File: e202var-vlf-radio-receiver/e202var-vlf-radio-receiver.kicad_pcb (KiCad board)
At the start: 2 copper layers, 0 parts

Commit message: Rough part placement. Created README. Images made by gerbv are off-center.
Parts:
- added BNC1: 12/18V, Wickerlib:CONN-BNC-TECONN-1-1634612-0, F.Cu at (106.1, 110.5)
- added BNC2: ANT IN, Wickerlib:CONN-BNC-TECONN-1-1634612-0, F.Cu at (107.4, 47.0)
- added BNC3: LINE IN/OUT, Wickerlib:CONN-BNC-TECONN-1-1634612-0, F.Cu at (106.1, 94.0)
- added C1: 33nF, Wickerlib:CAP-DISC-D7.5MM-P5MM, F.Cu at (65.3, 91.7)
- added C10: 10nF, Wickerlib:CAP-DISC-D3MM-P2.5MM, F.Cu at (89.9, 64.5)
- added C11: 100nF, Wickerlib:CAP-DISC-D7.5MM-P5MM, F.Cu at (72.6, 103.1)
- added C12: 10uF, Wickerlib:CAP-DISC-D3MM-P2.5MM, F.Cu at (80.5, 98.3)
- added C13: 100uF, Wickerlib:CAP-DISC-D7.5MM-P5MM, F.Cu at (65.3, 85.3)
- added C15: 150pF, Wickerlib:CAP-DISC-D3MM-P2.5MM, F.Cu at (82.5, 65.3)
- added C16: 4.7nF, Wickerlib:CAP-DISC-D7.5MM-P5MM, F.Cu at (64.8, 102.9)
- added C2: 100nF, Wickerlib:CAP-DISC-D7.5MM-P5MM, F.Cu at (72.7, 51.3)
- added C3: 8.2pF, Wickerlib:CAP-DISC-D7.5MM-P5MM, F.Cu at (62.7, 67.1)
- added C4: 10uF, Wickerlib:CAP-DISC-D3MM-P2.5MM, F.Cu at (74.2, 83.3)
- added C5: 150pF, Wickerlib:CAP-DISC-D3MM-P2.5MM, F.Cu at (86.6, 89.4)
- added C6: 10uF, Wickerlib:CAP-DISC-D3MM-P2.5MM, F.Cu at (103.6, 77.5)
- added C7: 4.7nF, Wickerlib:CAP-DISC-D7.5MM-P5MM, F.Cu at (99.3, 81.8)
- added C8: 150pF, Wickerlib:CAP-DISC-D3MM-P2.5MM, F.Cu at (61.7, 73.2)
- added C9: 100uF, Wickerlib:CAP-DISC-D7.5MM-P5MM, F.Cu at (98.0, 60.2)
- added D1: 1N4001, Wickerlib:DIODE-DO-41, F.Cu at (82.6, 115.8)
- added D2: 1N4001, Wickerlib:DIODE-DO-41, F.Cu at (95.5, 99.1)
- added D3: BLUE, Wickerlib:LED-D5MM-2PIN, F.Cu at (67.3, 114.8)
- added J1: 9V, Wickerlib:CONN-BARREL-JACK-2.5x5.5MM-TH, F.Cu at (60.9, 111.1)
- added J2: ON/OFF, Wickerlib:CONN-ONSHORE-SCREW-GREEN-2PIN-TH, F.Cu at (75.2, 114.6)
- added J3: HEADPHONES, Wickerlib:SJ1-3523N, F.Cu at (109.2, 60.7)
- added J4: 12V/18V, Wickerlib:CONN-BARREL-JACK-2.5x5.5MM-TH, F.Cu at (90.7, 109.5)
- added J5: FILTER, Wickerlib:CONN-ONSHORE-SCREW-GREEN-2PIN-TH, F.Cu at (57.1, 101.1)
- added L1: 3.3UH, Wickerlib:IND-78F-AXIAL, F.Cu at (76.5, 50.8)
- added LAMP1: NEON, Wickerlib:CONN-HEADER-STRAIGHT-P2.54MM-1x02, F.Cu at (93.7, 51.1)
- added Q1: BC547, Wickerlib:TO-92-INLINE-NARROW-OVAL, F.Cu at (74.2, 96.0)
- added Q2: BC547, Wickerlib:TO-92-INLINE-NARROW-OVAL, F.Cu at (63.5, 56.4)
- added R1: 10M, Wickerlib:RES-CARBONFILM-7MM, F.Cu at (79.0, 56.4)
- added R10: 10K, Wickerlib:RES-TRIMPOT-TTELEC-P160-TH, F.Cu at (111.8, 72.4)
- added R11: 4.7K, Wickerlib:RES-CARBONFILM-7MM, F.Cu at (90.2, 98.6)
- added R12: 2.2K, Wickerlib:RES-CARBONFILM-7MM, F.Cu at (73.2, 108.7)
- added R13: 1K, Wickerlib:RES-CARBONFILM-7MM, F.Cu at (69.8, 103.9)
- added R17: 33, Wickerlib:RES-CARBONFILM-7MM, F.Cu at (67.6, 78.5)
- added R2: 100K, Wickerlib:RES-CARBONFILM-7MM, F.Cu at (70.9, 40.4)
- added R3: 100K, Wickerlib:RES-CARBONFILM-7MM, F.Cu at (83.1, 69.3)
- added R4: 3.3k, Wickerlib:RES-CARBONFILM-7MM, F.Cu at (69.3, 85.1)
- added R5: 10M, Wickerlib:RES-CARBONFILM-7MM, F.Cu at (80.0, 45.2)
- added R6: 100K, Wickerlib:RES-CARBONFILM-7MM, F.Cu at (84.1, 50.5)
- added R7: 10, Wickerlib:RES-CARBONFILM-7MM, F.Cu at (84.3, 59.9)
- added R8: 10K, Wickerlib:RES-CARBONFILM-7MM, F.Cu at (95.2, 82.8)
- added R9: 33, Wickerlib:RES-CARBONFILM-7MM, F.Cu at (91.7, 55.4)
- added SMA1: ANT IN, Wickerlib:CONN-SMA-STRAIGHT-TH, F.Cu at (94.5, 43.2)
- added U1: MC7809, Wickerlib:TO-220-NEUTRAL123-VERT-LONGPADS, F.Cu at (90.7, 104.9)
- added U2: TLE2426, Wickerlib:TO-92-INLINE-NARROW-OVAL, F.Cu at (74.4, 91.2)
- added U3: NJM386, Wickerlib:DIP-8-W7.62MM-LONGPADS, F.Cu at (69.3, 63.0)
- added U4: TL081CP, Wickerlib:DIP-8-W7.62MM-LONGPADS, F.Cu at (81.3, 76.7)
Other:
- board outline added: 55.9 x 81.3 mm

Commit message: Added parts. Ready for layout.
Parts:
- added REF**: HOLE-PLATED-3.2MM, Wickerlib:HOLE-PLATED-3.2MM, F.Cu at (85.1, 33.5)
- added REF**: HOLE-PLATED-3.2MM, Wickerlib:HOLE-PLATED-3.2MM, F.Cu at (91.4, 33.5)
- added REF**: HOLE-PLATED-3.2MM, Wickerlib:HOLE-PLATED-3.2MM, F.Cu at (97.8, 33.5)
- L1: footprint Wickerlib:IND-78F-AXIAL -> Wickerlib:RES-CARBONFILM-7MM
- moved J3 4.32 mm to (107.2, 64.5)
- moved SMA1 3.75 mm to (91.2, 45.0)
- moved L1 2.65 mm to (75.7, 48.3), turned to 180 degrees
- moved LAMP1 2.50 mm to (96.0, 52.1)
- moved BNC2 1.05 mm to (106.7, 46.2)
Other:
- board text added: "12/9/2016"
- board text added: "E202VAR VLF Natural Radio Receiver"
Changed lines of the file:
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@@
 (kicad_pcb (version 4) (host pcbnew 4.0.4+e1-6308~48~ubuntu16.04.1-stable)
   (general
-    (links 87)
-    (no_connects 87)
-    (area 0 0 0 0)
+    (links 94)
+    (no_connects 94)
+    (area 58.343799 38.023799 114.376201 119.456201)
     (thickness 1.6)
-    (drawings 22)
+    (drawings 28)
     (tracks 0)
     (zones 0)
-    (modules 49)
+    (modules 52)
     (nets 33)
   )
@@
   )
   (module Wickerlib:CONN-BNC-TECONN-1-1634612-0 (layer F.Cu)
-    (at 107.4166 46.96968 270)
+    (at 106.6546 46.24578 270)
     (descr "BNC Socket TYCO AMP")
     (tags "BNC Socket TYCO AMP")
@@
       (net 29 "Net-(J1-Pad1)"))
   )
-  (module Wickerlib:SJ1-3523N (layer F.Cu)
-    (at 109.22 60.706)
-    (fp_text reference J3 (at 0 0.5) (layer F.SilkS)
-      (effects (font (size 1 1) (thickness 0.15)))
-    )
-    (fp_text value HEADPHONES (at 0 -0.5) (layer F.Fab)
-      (effects (font (size 1 1) (thickness 0.15)))
-    )
-  )
   (module Wickerlib:CONN-BARREL-JACK-2.5x5.5MM-TH (layer F.Cu)
     (at 90.651 109.5224 90)
@@
       (net 5 +2V))
   )
-  (module Wickerlib:IND-78F-AXIAL (layer F.Cu)
-    (at 76.454 50.8)
-    (fp_text reference L1 (at 7.112 -0.254) (layer F.SilkS)
-      (effects (font (size 1 1) (thickness 0.15)))
-    )
-    (fp_text value 3.3UH (at 0 -0.5) (layer F.Fab)
-      (effects (font (size 1 1) (thickness 0.15)))
-    )
-  )
   (module Wickerlib:CONN-HEADER-STRAIGHT-P2.54MM-1x02 (layer F.Cu)
-    (at 93.726 51.054 270)
+    (at 96.012 52.07 270)
     (descr "Through hole pin header")
     (tags "pin header")
@@
   )
   (module Wickerlib:CONN-SMA-STRAIGHT-TH (layer F.Cu)
-    (at 94.488 43.18)
+    (at 91.186 44.958)
     (descr "SMA pcb mounting jack")
     (tags "SMA Jack  Striaght")
@@
     (pad 8 thru_hole oval (at 7.62 0) (size 2.3 1.6) (drill 0.8) (layers *.Cu *.Mask F.SilkS))
   )
+  (module Wickerlib:RES-CARBONFILM-7MM (layer F.Cu)
+    (at 75.692 48.26 180)
+    (descr "Resistor, Axial,  RM 7.62mm, 1/3W,")
+    (tags "Resistor Axial RM 7.62mm 1/3W R3")
+    (fp_text reference L1 (at 3.8 0 180) (layer F.Fab)
+      (effects (font (size 1 1) (thickness 0.15)))
+    )
+    (fp_text value 3.3UH (at 3.81 3.81 180) (layer F.Fab) hide
+      (effects (font (size 1 1) (thickness 0.15)))
+    )
+    (fp_text user %R (at 3.9 -2.3 180) (layer F.SilkS)
+      (effects (font (size 1 1) (thickness 0.15)))
+    )
+    (fp_line (start 8.9 -1.5) (end -1.3 -1.5) (layer F.Fab) (width 0.0508))
+    (fp_line (start 8.9 1.5) (end 8.9 -1.5) (layer F.Fab) (width 0.0508))
+    (fp_line (start 8.8 1.5) (end 8.9 1.5) (layer F.Fab) (width 0.0508))
+    (fp_line (start -1.3 1.5) (end 8.8 1.5) (layer F.Fab) (width 0.0508))
+    (fp_line (start -1.3 -1.5) (end -1.3 1.5) (layer F.Fab) (width 0.0508))
+    (fp_line (start -1.25 -1.5) (end 8.85 -1.5) (layer F.CrtYd) (width 0.05))
+    (fp_line (start -1.25 1.5) (end -1.25 -1.5) (layer F.CrtYd) (width 0.05))
+    (fp_line (start 8.85 -1.5) (end 8.85 1.5) (layer F.CrtYd) (width 0.05))
+    (fp_line (start -1.25 1.5) (end 8.85 1.5) (layer F.CrtYd) (width 0.05))
+    (fp_line (start 1.27 -1.27) (end 6.35 -1.27) (layer F.SilkS) (width 0.15))
+    (fp_line (start 6.35 -1.27) (end 6.35 1.27) (layer F.SilkS) (width 0.15))
+    (fp_line (start 6.35 1.27) (end 1.27 1.27) (layer F.SilkS) (width 0.15))
+    (fp_line (start 1.27 1.27) (end 1.27 -1.27) (layer F.SilkS) (width 0.15))
+    (pad 1 thru_hole circle (at 0 0 180) (size 1.99898 1.99898) (drill 1.00076) (layers *.Cu *.SilkS *.Mask)
+      (net 3 "Net-(BNC2-Pad1)"))
+    (pad 2 thru_hole circle (at 7.62 0 180) (size 1.99898 1.99898) (drill 1.00076) (layers *.Cu *.SilkS *.Mask)
+      (net 7 "Net-(C2-Pad2)"))
+  )
+  (module Wickerlib:HOLE-PLATED-3.2MM (layer F.Cu)
+    (at 85.09 33.528)
+    (fp_text reference REF** (at 0 0) (layer F.Fab)
+      (effects (font (size 1 1) (thickness 0.15)))
+    )
+    (fp_text value HOLE-PLATED-3.2MM (at 0 -0.5) (layer F.Fab) hide
+      (effects (font (size 1 1) (thickness 0.15)))
+    )
+    (fp_circle (center 0 0) (end 2.54 1.27) (layer F.Fab) (width 0.04064))
+    (pad 1 thru_hole circle (at 0 0) (size 5 5) (drill 3.2) (layers *.Cu *.Mask))
+  )
+  (module Wickerlib:HOLE-PLATED-3.2MM (layer F.Cu)
+    (at 91.44 33.528)
+    (fp_text reference REF** (at 0 0) (layer F.Fab)
+      (effects (font (size 1 1) (thickness 0.15)))
+    )
+    (fp_text value HOLE-PLATED-3.2MM (at 0 -0.5) (layer F.Fab) hide
+      (effects (font (size 1 1) (thickness 0.15)))
+    )
+    (fp_circle (center 0 0) (end 2.54 1.27) (layer F.Fab) (width 0.04064))
+    (pad 1 thru_hole circle (at 0 0) (size 5 5) (drill 3.2) (layers *.Cu *.Mask))
+  )
+  (module Wickerlib:HOLE-PLATED-3.2MM (layer F.Cu)
+    (at 97.79 33.528)
+    (fp_text reference REF** (at 0 0) (layer F.Fab)
+      (effects (font (size 1 1) (thickness 0.15)))
+    )
+    (fp_text value HOLE-PLATED-3.2MM (at 0 -0.5) (layer F.Fab) hide
+      (effects (font (size 1 1) (thickness 0.15)))
+    )
+    (fp_circle (center 0 0) (end 2.54 1.27) (layer F.Fab) (width 0.04064))
+    (pad 1 thru_hole circle (at 0 0) (size 5 5) (drill 3.2) (layers *.Cu *.Mask))
+  )
+  (module Wickerlib:SJ1-3523N (layer F.Cu)
+    (at 107.188 64.516)
+    (fp_text reference J3 (at 1.27 -2.413) (layer F.Fab)
+      (effects (font (size 1 1) (thickness 0.15)))
+    )
+    (fp_text value HEADPHONES (at 0 -0.5) (layer F.Fab) hide
+      (effects (font (size 1 1) (thickness 0.15)))
+    )
+    (fp_text user %R (at -1.778 -9.779) (layer F.SilkS)
+      (effects (font (size 1 1) (thickness 0.15)))
+    )
+    (fp_line (start -3.81 3.81) (end 6.35 3.81) (layer F.CrtYd) (width 0.04064))
+    (fp_line (start -3.81 -8.89) (end -3.81 3.81) (layer F.CrtYd) (width 0.04064))
+    (fp_line (start 6.35 -8.89) (end -3.81 -8.89) (layer F.CrtYd) (width 0.04064))
+    (fp_line (start 6.35 3.81) (end 6.35 -8.89) (layer F.CrtYd) (width 0.04064))
+    (fp_line (start -3.81 3.81) (end 6.35 3.81) (layer F.Fab) (width 0.04064))
+    (fp_line (start -3.81 -8.89) (end -3.81 3.81) (layer F.Fab) (width 0.04064))
+    (fp_line (start 6.35 -8.89) (end -3.81 -8.89) (layer F.Fab) (width 0.04064))
+    (fp_line (start 6.35 -8.89) (end 6.35 3.81) (layer F.Fab) (width 0.04064))
+    (fp_line (start -3.81 3.81) (end 6.35 3.81) (layer F.SilkS) (width 0.1524))
+    (fp_line (start -3.81 -8.89) (end -3.81 3.81) (layer F.SilkS) (width 0.1524))
+    (fp_line (start 6.35 -8.89) (end -3.81 -8.89) (layer F.SilkS) (width 0.1524))
+    (fp_line (start 6.35 3.81) (end 6.35 -8.89) (layer F.SilkS) (width 0.1524))
+    (pad 4 thru_hole circle (at 5.08 -7.62) (size 2.1844 2.1844) (drill 1.2954) (layers *.Cu *.Mask)
+      (net 1 GND))
+    (pad 3 thru_hole circle (at 5.08 -5.08) (size 2.1844 2.1844) (drill 1.2954) (layers *.Cu *.Mask)
+      (net 1 GND))
+    (pad "" np_thru_hole circle (at 5.08 -2.54) (size 1.2954 1.2954) (drill 1.2954) (layers *.Cu))
+    (pad 2 thru_hole circle (at 5.08 0) (size 2.1844 2.1844) (drill 1.2954) (layers *.Cu *.Mask)
+      (net 17 "Net-(C9-Pad1)"))
+    (pad 1 thru_hole circle (at 5.08 2.54) (size 2.1844 2.1844) (drill 1.2954) (layers *.Cu *.Mask)
+      (net 17 "Net-(C9-Pad1)"))
+    (pad 5 thru_hole circle (at 0 -2.54) (size 2.1844 2.1844) (drill 1.2954) (layers *.Cu *.Mask)
+      (net 1 GND))
+    (pad "" np_thru_hole circle (at 0 -7.62) (size 1.2954 1.2954) (drill 1.2954) (layers *.Cu))
+    (pad "" np_thru_hole circle (at -2.54 -7.62) (size 1.2954 1.2954) (drill 1.2954) (layers *.Cu))
+    (pad "" np_thru_hole circle (at 0 2.54) (size 1.2954 1.2954) (drill 1.2954) (layers *.Cu))
+    (pad "" np_thru_hole circle (at -2.54 2.54) (size 1.2954 1.2954) (drill 1.2954) (layers *.Cu))
+  )
+  (gr_text 12/9/2016 (at 109.22 30.734) (layer F.Fab)
+    (effects (font (size 1.016 1.016) (thickness 0.1524)))
+  )
+  (gr_text "E202VAR VLF Natural Radio Receiver" (at 99.568 28.702) (layer F.Fab)
+    (effects (font (size 1.016 1.016) (thickness 0.1524)))
+  )
+  (gr_line (start 58.42 38.1) (end 114.3 38.1) (layer F.Fab) (width 0.1524))
+  (gr_line (start 58.42 119.38) (end 58.42 38.1) (layer F.Fab) (width 0.1524))
+  (gr_line (start 114.3 119.38) (end 58.42 119.38) (layer F.Fab) (width 0.1524))
+  (gr_line (start 114.3 38.1) (end 114.3 119.38) (layer F.Fab) (width 0.1524))
   (gr_line (start 113.03 38.1) (end 114.3 38.1) (layer Edge.Cuts) (width 0.1524))
   (gr_line (start 58.42 38.1) (end 113.03 38.1) (layer Edge.Cuts) (width 0.1524))

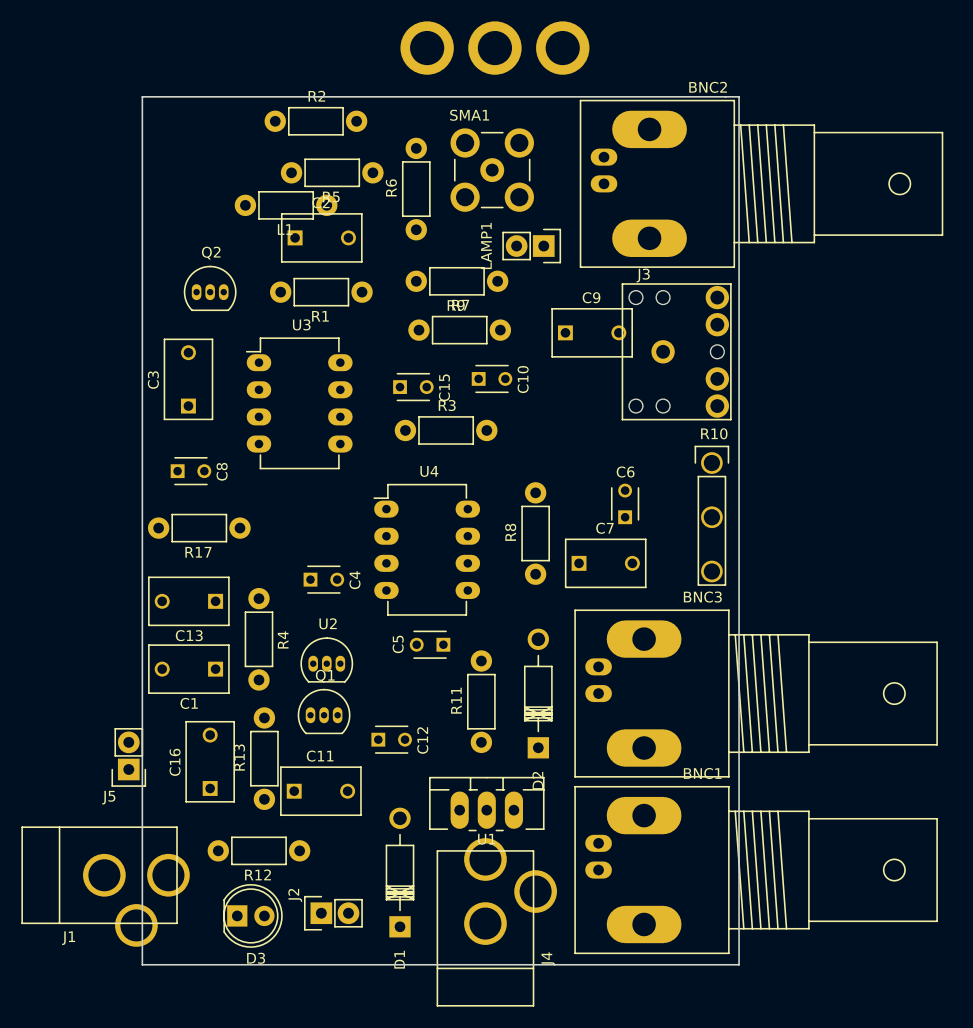
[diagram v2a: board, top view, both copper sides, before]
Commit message: Ported the board to KiCad.
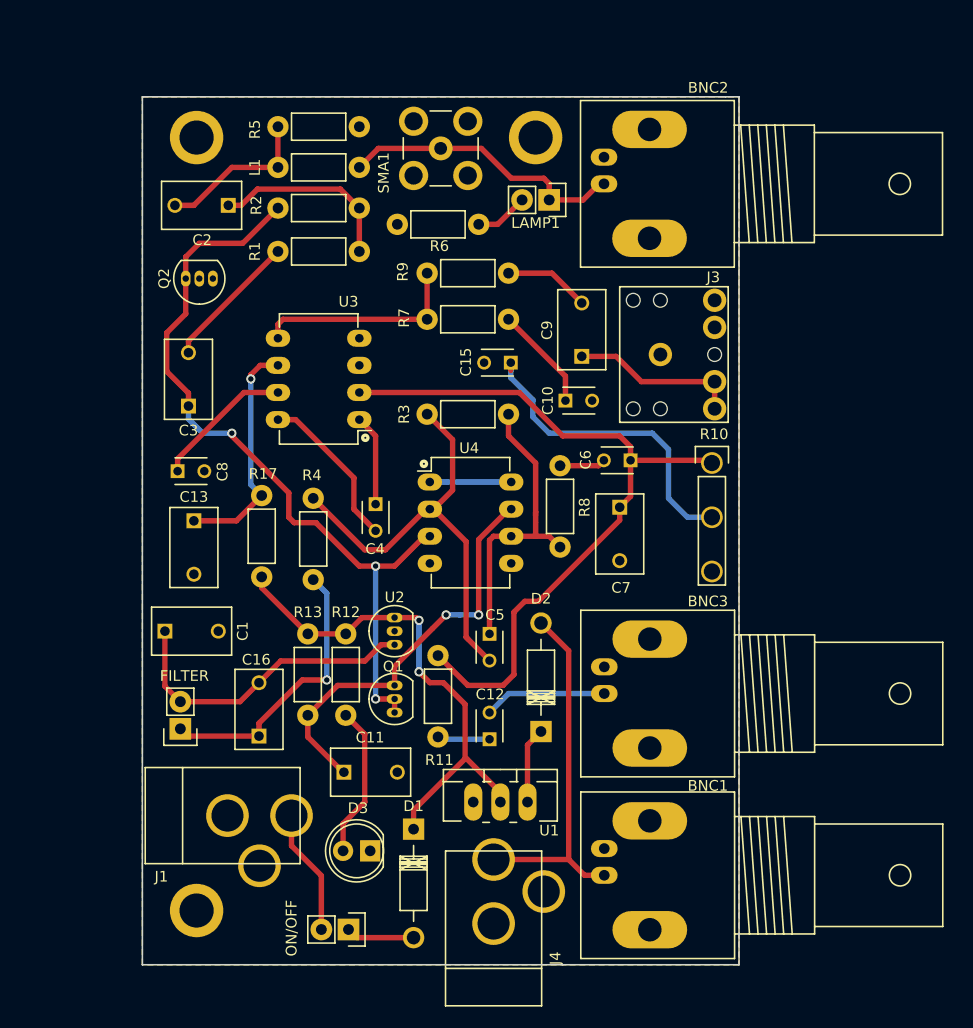
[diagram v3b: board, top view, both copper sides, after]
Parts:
- moved H3 85.5 mm to (63.5, 114.3)
- moved H2 23.2 mm to (63.5, 41.9)
- moved R12 20.8 mm to (77.5, 88.4), turned to 270 degrees
- moved R13 16.0 mm to (73.9, 88.4), turned to 270 degrees
- moved D3 13.9 mm to (79.8, 108.7), turned to 180 degrees
- moved J1 12.8 mm to (72.4, 105.5)
- moved U3 10.8 mm to (78.7, 68.3), turned to 180 degrees
- moved R4 10.7 mm to (74.4, 75.7)
- moved C15 10.6 mm to (92.9, 63.0), turned to 180 degrees
- moved C12 10.4 mm to (90.9, 98.3), turned to 90 degrees
- moved R8 10.4 mm to (97.5, 72.6), turned to 270 degrees
- moved R5 9.88 mm to (71.1, 40.9), turned to 0 degrees
- moved C4 9.34 mm to (80.3, 76.2), turned to 270 degrees
- moved D1 9.23 mm to (83.8, 106.7), turned to 270 degrees
- moved H1 8.76 mm to (95.2, 41.9)
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- renumbered REF** to H1, REF** to H2, REF** to H3
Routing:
- net Net-(C3-Pad1): track 0.00 -> 73.7 mm, vias 0 -> 3
- net Net-(C6-Pad1): track 0.00 -> 70.5 mm
- net +9V: track 0.00 -> 47.9 mm, vias 0 -> 2
- net Net-(C5-Pad2): track 0.00 -> 41.8 mm
- net Net-(C11-Pad1): track 0.00 -> 39.0 mm, vias 0 -> 2
- net Net-(BNC1-Pad1): track 0.00 -> 34.2 mm
- net Net-(C15-Pad1): track 0.00 -> 30.5 mm
- net +2V: track 0.00 -> 29.5 mm
- net Net-(C5-Pad1): track 0.00 -> 29.1 mm
- net Net-(BNC2-Pad1): track 0.00 -> 27.2 mm
- net Net-(C16-Pad1): track 0.00 -> 26.8 mm, vias 0 -> 1
- net Net-(C13-Pad1): track 0.00 -> 22.0 mm, vias 0 -> 1
- net Net-(R7-Pad1): track 0.00 -> 19.8 mm
- net Net-(C2-Pad1): track 0.00 -> 17.7 mm
- net Net-(C9-Pad1): track 0.00 -> 16.0 mm
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- added copper zone on B.Cu, net GND
- added copper zone on F.Cu, net GND
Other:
- board text added: "E202VAR VLF Radio Receiver"
- board text added: "ON/OFF"
- board text added: "v1.2"
- board text added: "v1.2 12/9/2016"
- board text added: "wickerbox.net"
- board text removed: "12/9/2016"
